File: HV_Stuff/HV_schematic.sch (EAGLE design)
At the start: 7 parts

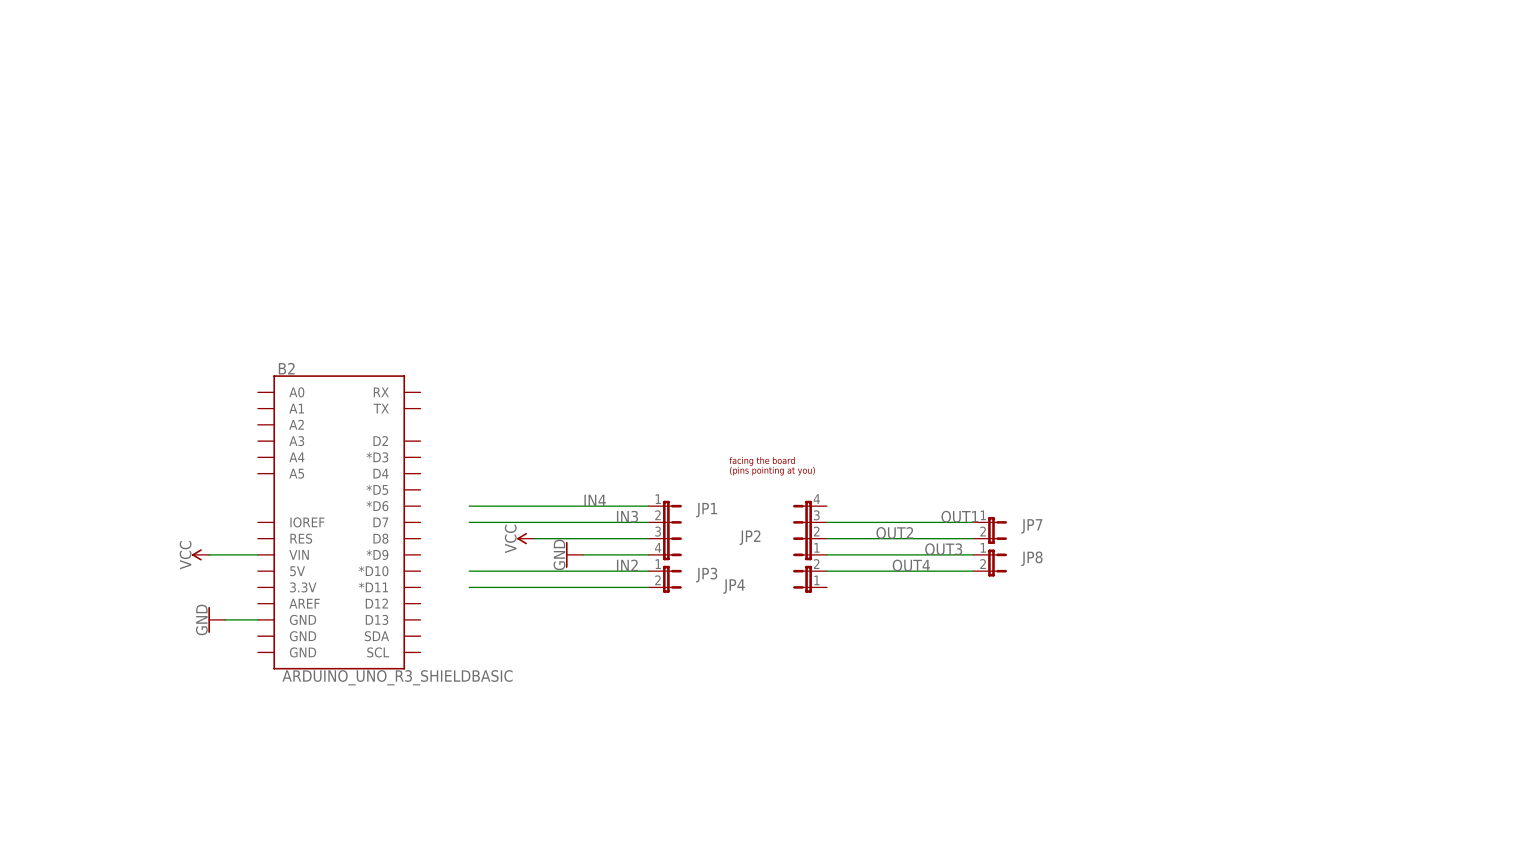
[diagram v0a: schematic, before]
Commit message: Changed to mega
Got schematic and PCB running on a mega
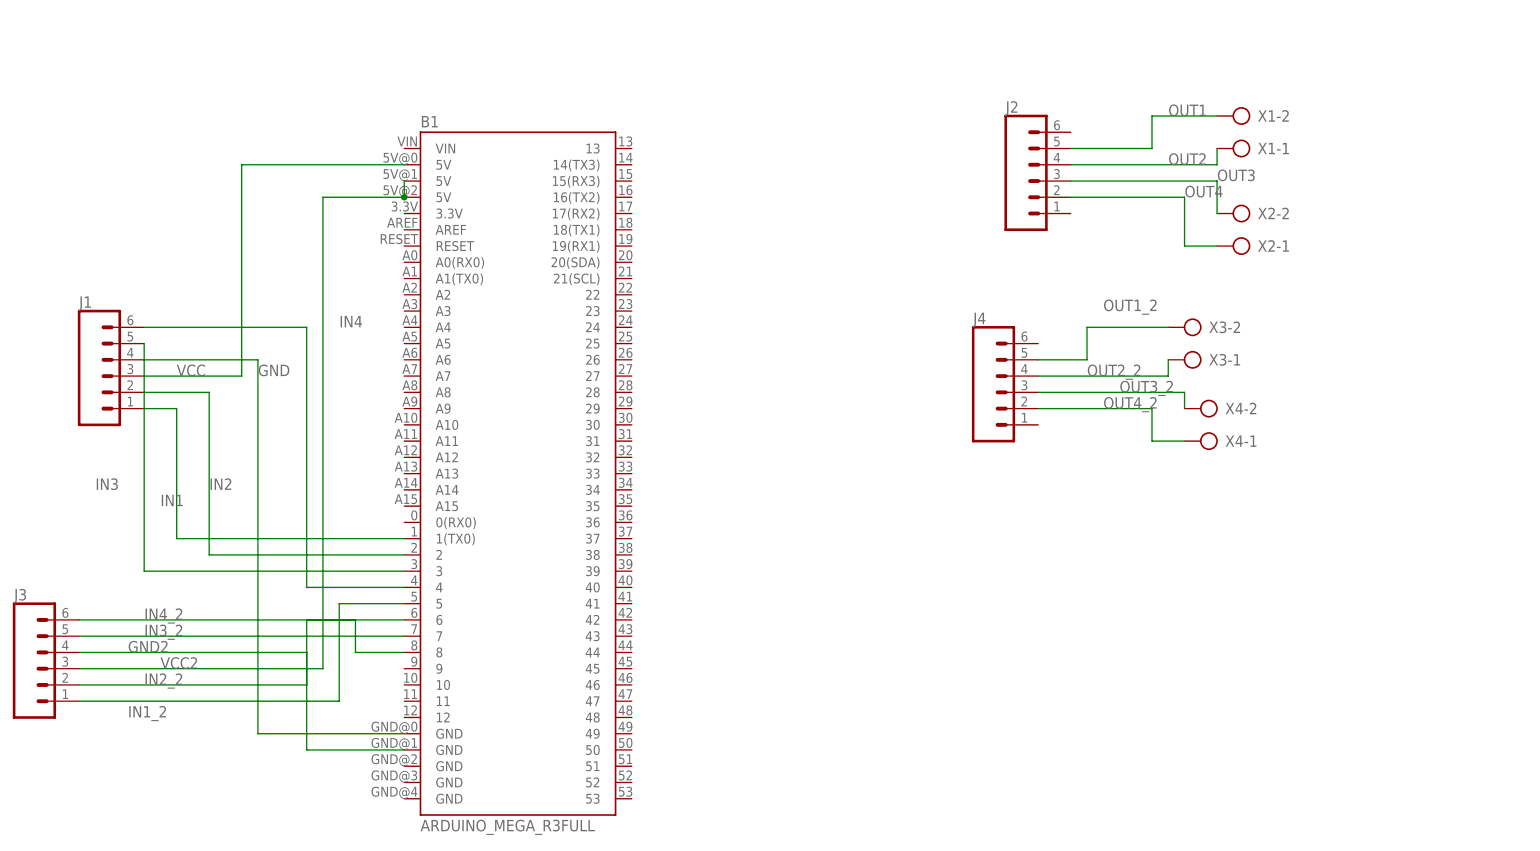
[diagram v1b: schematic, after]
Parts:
- removed B2: ARDUINO_UNO_R3_SHIELDBASIC, SparkFun-Boards:ARDUINO_UNO_R3_SHIELDBASIC
- removed JP1, JP2: (no value), jumper:JP4E
- removed JP3, JP4, JP7, JP8: (no value), jumper:JP1E
- added B1: ARDUINO_MEGA_R3FULL, SparkFun-Boards:ARDUINO_MEGA_R3FULL
- added J1, J2, J3, J4: (no value), SparkFun-Connectors:CONN_06LONGPADS
- added X1, X2, X3, X4: (no value), con-ptr500:AK500/2
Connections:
- new net GND2: B1.GND@1, J3.4
- new net IN1_2: B1.5, J3.1
- new net IN2_2: B1.6, J3.2
- new net IN3_2: B1.7, J3.5
- new net IN4_2: B1.8, J3.6
- new net OUT1_2: J4.5, X3-2.KL
- new net OUT2_2: J4.4, X3-1.KL
- new net OUT3_2: J4.3, X4-2.KL
- new net OUT4_2: J4.2, X4-1.KL
- new net VCC2: B1.5V@1, B1.5V@2, J3.3
- net GND: now also B1.GND@0, J1.4; no longer B2.GND@2, JP1.4
- net IN1: now also B1.1(TX0), J1.1; no longer JP3.2
- net IN2: now also B1.2, J1.2; no longer JP3.1
- net IN3: now also B1.3, J1.5; no longer JP1.2
- net IN4: now also B1.4, J1.6; no longer JP1.1
- net OUT1: now also J2.5, X1-2.KL; no longer JP2.3, JP7.1
- net OUT2: now also J2.4, X1-1.KL; no longer JP2.2, JP7.2
- net OUT3: now also J2.3, X2-2.KL; no longer JP2.1, JP8.1
- net OUT4: now also J2.2, X2-1.KL; no longer JP4.2, JP8.2
- net VCC: now also B1.5V@0, J1.3; no longer B2.VIN, JP1.3
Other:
- note removed: "facing the board (pins pointing at you)"

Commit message: Made it, it's gorgeous. It looks very pretty
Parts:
- removed X1, X2, X3, X4: (no value), con-ptr500:AK500/2
- added M1, M2, M3, M4: (no value), con-ptr500:AK500/2
- B1: device SparkFun-Boards:ARDUINO_MEGA_R3FULL -> Will Library:ARDUINO_MEGA_R3FULL
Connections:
- net IN1 renamed IN1_1
- net IN2 renamed IN2_1
- net IN3 renamed IN3_1
- net IN4 renamed IN4_1
- removed net GND: B1.GND@0, J1.4
- removed net GND2: B1.GND@1, J3.4
- removed net OUT1: J2.5, X1-2.KL
- removed net OUT2: J2.4, X1-1.KL
- removed net OUT3: J2.3, X2-2.KL
- removed net OUT4: J2.2, X2-1.KL
- removed net VCC: B1.5V@0, J1.3
- removed net VCC2: B1.5V@1, B1.5V@2, J3.3
- new net 5V_1: B1.5V@2, J1.3
- new net 5V_2: B1.5V@0, J3.3
- new net GND_1: B1.GND@3, J1.4
- new net GND_2: B1.GND@4, J3.4
- new net N$1: J2.3, M2-1.KL
- new net OUT1_1: J2.5, M1-1.KL
- new net OUT2_1: J2.4, M1-2.KL
- new net OUT4_1: J2.2, M2-2.KL
- net OUT1_2: now also M3-1.KL; no longer X3-2.KL
- net OUT2_2: now also M3-2.KL; no longer X3-1.KL
- net OUT3_2: now also M4-1.KL; no longer X4-2.KL
- net OUT4_2: now also M4-2.KL; no longer X4-1.KL
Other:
- moved on the sheet: B1, J1, J2, J3, J4
